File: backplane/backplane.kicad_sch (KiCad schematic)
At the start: 30 parts, among them J6 USB-C, U2 AP2112K-3.3

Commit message: PDFs of schematics, readme updates
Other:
- company: (none) -> Team Rebellion
- title: (none) -> RV4028 Backplane
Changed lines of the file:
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@@
 	(generator_version "9.0")
 	(paper "A3")
+	(title_block
+		(title "RV4028 Backplane")
+		(date "2026-01-22")
+		(rev "v0.1")
+		(company "Team Rebellion")
+	)
 	(junction
 		(at 92.71 38.1)

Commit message: Backplane reset and fixes
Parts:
- added R5: 47k, Resistor_SMD:R_0402_1005Metric, symbol Device:R
- added R6: 1k, Resistor_SMD:R_0402_1005Metric, symbol Device:R
- added SW1: RESET, RV4028:SW-SMD_HX-TS-1101-C-W, symbol Switch:SW_Push
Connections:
- net +3V3: now also R5.1
- net GND: now also R6.1
- net ~{RST}: now also R5.2, SW1.2
- new net: R6.2, SW1.1

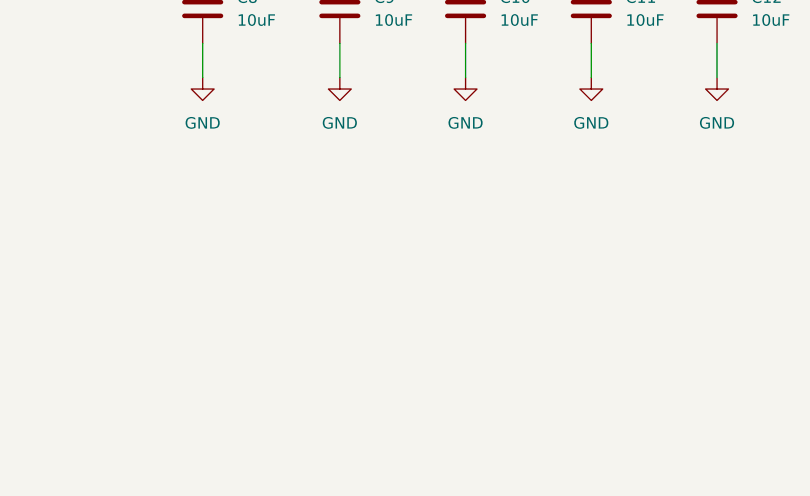
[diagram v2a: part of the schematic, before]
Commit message: Mounting holes
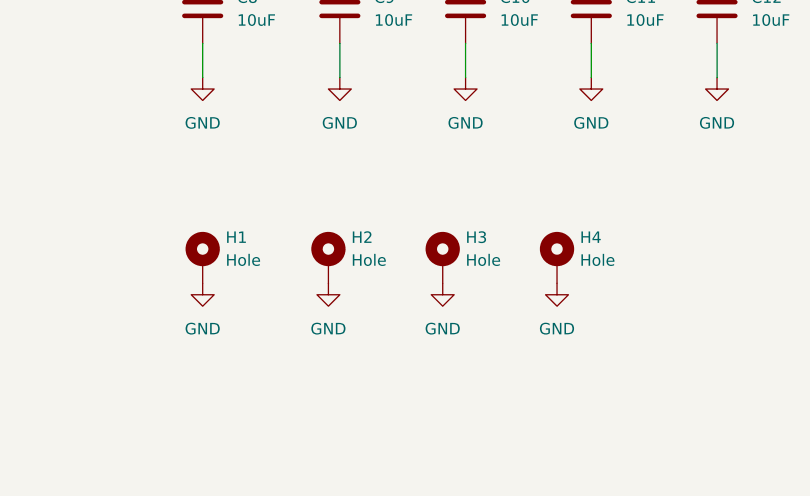
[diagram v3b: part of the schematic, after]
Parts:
- added H1, H2, H3, H4: Hole, MountingHole:MountingHole_2.7mm_M2.5_DIN965_Pad, symbol Mechanical:MountingHole_Pad
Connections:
- net GND: now also H1.1, H2.1, H3.1, H4.1
